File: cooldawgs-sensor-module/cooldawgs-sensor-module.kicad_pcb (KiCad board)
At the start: 2 copper layers, 1 part, among them U1 XIAO-nRF52840-DIP

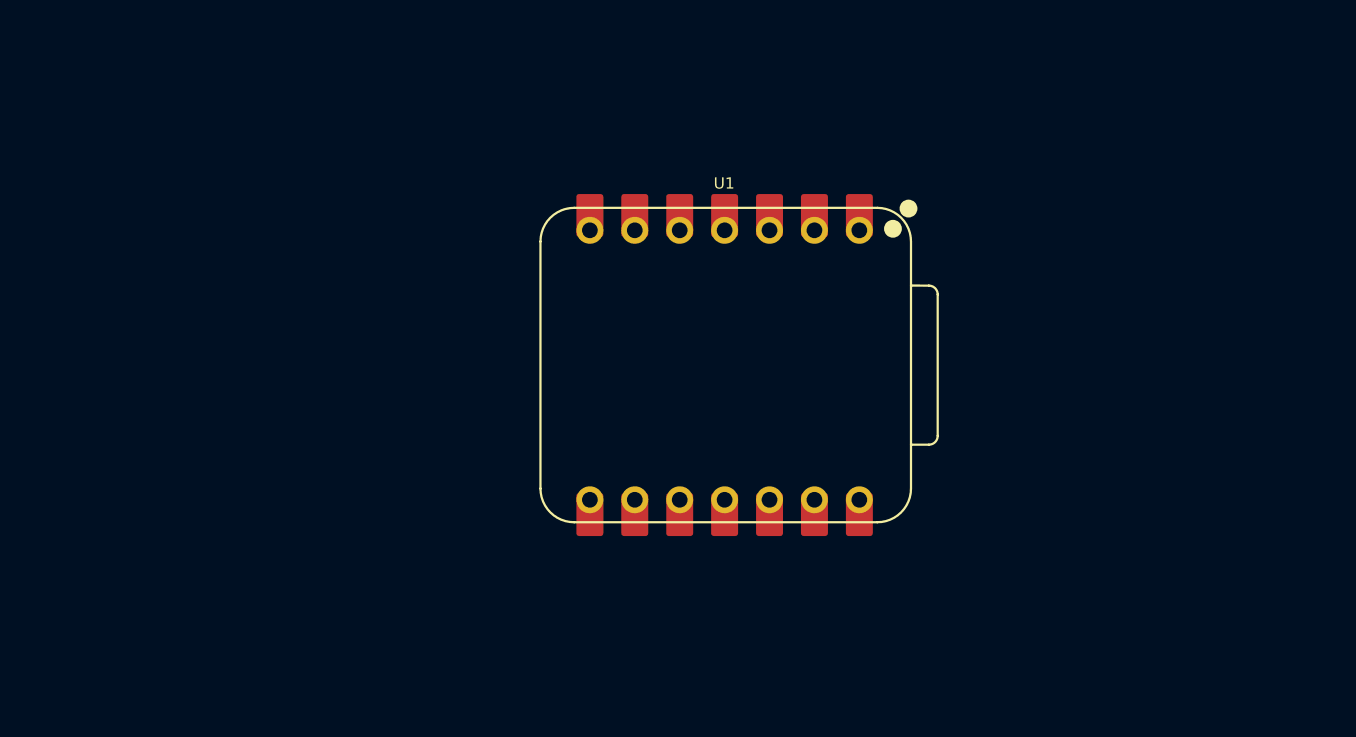
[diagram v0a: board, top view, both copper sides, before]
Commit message: added all sensors and created initial pcb
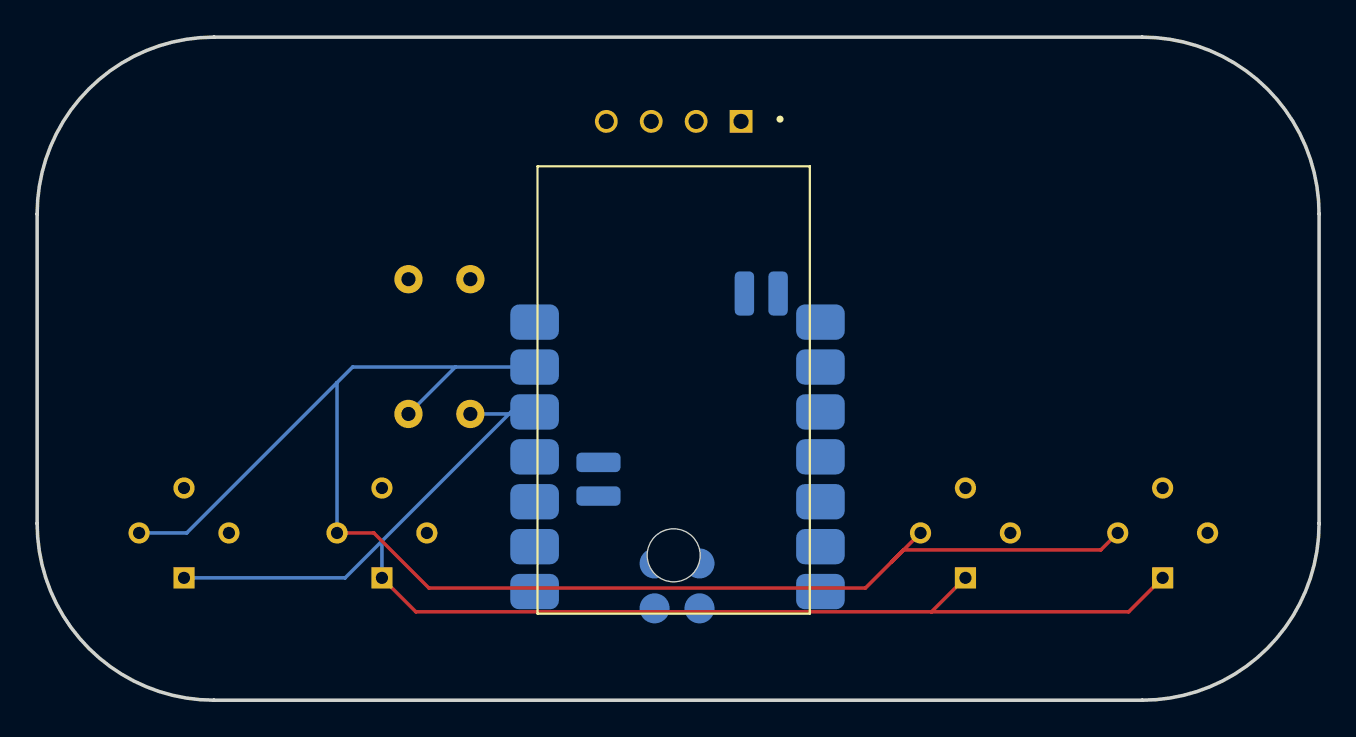
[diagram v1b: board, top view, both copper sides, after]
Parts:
- added R1: R, Resistor_THT:R_Axial_DIN0207_L6.3mm_D2.5mm_P7.62mm_Horizontal, B.Cu at (105.5, 86.2)
- added R2: R, Resistor_THT:R_Axial_DIN0207_L6.3mm_D2.5mm_P7.62mm_Horizontal, B.Cu at (109.0, 86.2)
- added U2: MLX90614ESF-AAA-000-TU, MLX90614ESF-AAA-000-TU:TO254P912H435-4, B.Cu at (104.0, 100.5)
- added U3: DHT22, DHT22:XDCR_DHT22, F.Cu at (120.5, 92.5)
- added U4: MLX90614ESF-AAA-000-TU, MLX90614ESF-AAA-000-TU:TO254P912H435-4, B.Cu at (92.8, 100.5)
- added U5: MLX90614ESF-AAA-000-TU, MLX90614ESF-AAA-000-TU:TO254P912H435-4, B.Cu at (148.2, 100.5)
- added U6: MLX90614ESF-AAA-000-TU, MLX90614ESF-AAA-000-TU:TO254P912H435-4, B.Cu at (137.0, 100.5)
- U1: value XIAO-nRF52840-DIP -> XIAO-nRF52840-SMD; footprint XIAO_Series_Footprints:XIAO-nRF52840-DIP -> XIAO_Series_Footprints:XIAO-nRF52840-SMD; moved to B.Cu
- moved U1 12.7 mm to (111.8, 85.7)
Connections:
- U1 pad 12: unconnected-(U1-3V3-Pad12) -> +3.3V
- U1 pad 13: unconnected-(U1-GND-Pad13) -> GND
- U1 pad 2: unconnected-(U1-P0.03_A1_D1-Pad2) -> PWM
- U1 pad 5: unconnected-(U1-P0.04_A4_D4_SDA-Pad5) -> SDA
- U1 pad 6: unconnected-(U1-P0.05_A5_D5_SCL-Pad6) -> SCL
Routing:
- net SCL: track 0.00 -> 87.6 mm
- net SDA: track 0.00 -> 77.9 mm
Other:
- board outline added: 72.5 x 37.5 mm
- board text added: "Vipr CoolDawgs Sensor Module"
